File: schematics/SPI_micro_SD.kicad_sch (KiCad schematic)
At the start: 6 parts

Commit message: Файлы измененный Kicad
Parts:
- C0300: renamed from C204; footprint Capacitor_SMD:C_1206_3216Metric_Pad1.33x1.80mm_HandSolder -> Capacitor_SMD:C_0805_2012Metric
- renumbered R205 to R0300, R206 to R0301, R207 to R0302, R208 to R0303, MODULE2 to SD
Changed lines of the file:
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@@
 	(wire
 		(pts
-			(xy 140.97 102.87) (xy 146.05 102.87)
+			(xy 135.89 102.87) (xy 146.05 102.87)
 		)
 		(stroke
@@
 	(wire
 		(pts
-			(xy 140.97 100.33) (xy 146.05 100.33)
+			(xy 135.89 100.33) (xy 146.05 100.33)
 		)
 		(stroke
@@
 	(wire
 		(pts
-			(xy 140.97 107.95) (xy 146.05 107.95)
+			(xy 135.89 107.95) (xy 146.05 107.95)
 		)
 		(stroke
@@
 	(wire
 		(pts
-			(xy 140.97 113.03) (xy 146.05 113.03)
+			(xy 135.89 113.03) (xy 146.05 113.03)
 		)
 		(stroke
@@
 	(hierarchical_label "SPI_CS"
 		(shape bidirectional)
-		(at 140.97 100.33 180)
+		(at 135.89 100.33 180)
 		(effects
 			(font
@@
 	(hierarchical_label "SPI_MOSI"
 		(shape bidirectional)
-		(at 140.97 102.87 180)
+		(at 135.89 102.87 180)
 		(effects
 			(font
@@
 	(hierarchical_label "SPI_SCK"
 		(shape bidirectional)
-		(at 140.97 107.95 180)
+		(at 135.89 107.95 180)
 		(effects
 			(font
@@
 	(hierarchical_label "SPI_MISO"
 		(shape bidirectional)
-		(at 140.97 113.03 180)
+		(at 135.89 113.03 180)
 		(effects
 			(font
@@
 		(on_board yes)
 		(dnp no)
-		(property "Reference" "R206"
-			(at 143.764 101.6 90)
+		(property "Reference" "R0301"
+			(at 142.748 101.6 90)
 			(effects
 				(font
@@
 			(project "MasterBoard"
 				(path "/97e8f341-b455-4614-ab7f-cc310164e7aa/8aa098bc-8147-495f-9e0e-6764d1cf376d"
-					(reference "R206")
+					(reference "R0301")
 					(unit 1)
 				)
@@
 		(on_board yes)
 		(dnp no)
-		(property "Reference" "R207"
-			(at 143.764 106.68 90)
+		(property "Reference" "R0302"
+			(at 142.748 106.68 90)
 			(effects
 				(font
@@
 			(project "MasterBoard"
 				(path "/97e8f341-b455-4614-ab7f-cc310164e7aa/8aa098bc-8147-495f-9e0e-6764d1cf376d"
-					(reference "R207")
+					(reference "R0302")
 					(unit 1)
 				)
@@
 		(on_board yes)
 		(dnp no)
-		(property "Reference" "R205"
-			(at 143.764 99.06 90)
+		(property "Reference" "R0300"
+			(at 142.748 99.06 90)
 			(effects
 				(font
@@
 			(project "MasterBoard"
 				(path "/97e8f341-b455-4614-ab7f-cc310164e7aa/8aa098bc-8147-495f-9e0e-6764d1cf376d"
-					(reference "R205")
+					(reference "R0300")
 					(unit 1)
 				)
@@
 		(dnp no)
 		(fields_autoplaced yes)
-		(property "Reference" "C204"
+		(property "Reference" "C0300"
 			(at 118.11 109.855 0)
 			(effects
@@
 			)
 		)
-		(property "Footprint" "Capacitor_SMD:C_1206_3216Metric_Pad1.33x1.80mm_HandSolder"
+		(property "Footprint" "Capacitor_SMD:C_0805_2012Metric"
 			(at 113.3348 106.68 0)
 			(effects
@@
 			(project "MasterBoard"
 				(path "/97e8f341-b455-4614-ab7f-cc310164e7aa/8aa098bc-8147-495f-9e0e-6764d1cf376d"
-					(reference "C204")
+					(reference "C0300")
 					(unit 1)
 				)
@@
 		(on_board yes)
 		(dnp no)
-		(property "Reference" "R208"
-			(at 143.764 111.76 90)
+		(property "Reference" "R0303"
+			(at 142.748 111.76 90)
 			(effects
 				(font
@@
 			(project "MasterBoard"
 				(path "/97e8f341-b455-4614-ab7f-cc310164e7aa/8aa098bc-8147-495f-9e0e-6764d1cf376d"
-					(reference "R208")
+					(reference "R0303")
 					(unit 1)
 				)
@@
 		(on_board yes)
 		(dnp no)
-		(fields_autoplaced yes)
-		(property "Reference" "MODULE2"
-			(at 182.245 87.63 0)
+		(property "Reference" "SD"
+			(at 181.61 89.408 0)
 			(effects
 				(font
@@
 					(size 1.27 1.27)
 				)
+				(hide yes)
 			)
 		)
@@
 			(project "stm32f4_ILI_RS_SD"
 				(path "/97e8f341-b455-4614-ab7f-cc310164e7aa/8aa098bc-8147-495f-9e0e-6764d1cf376d"
-					(reference "MODULE2")
-					(unit 1)
-				)
+					(reference "SD")
+					(unit 1)
+				)

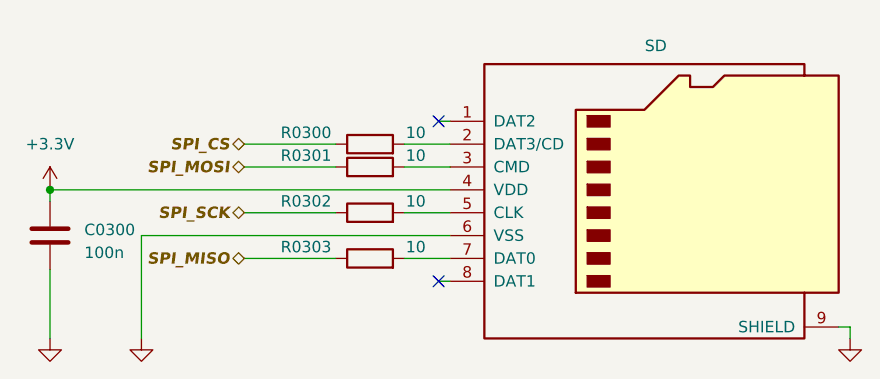
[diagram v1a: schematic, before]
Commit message: Прошелся по всей схеме: 1. почистил компоненты; 2. задал посадочные места; 3. Выставил все ссылки на плате в притык, дальнейшее расширение - смена мк
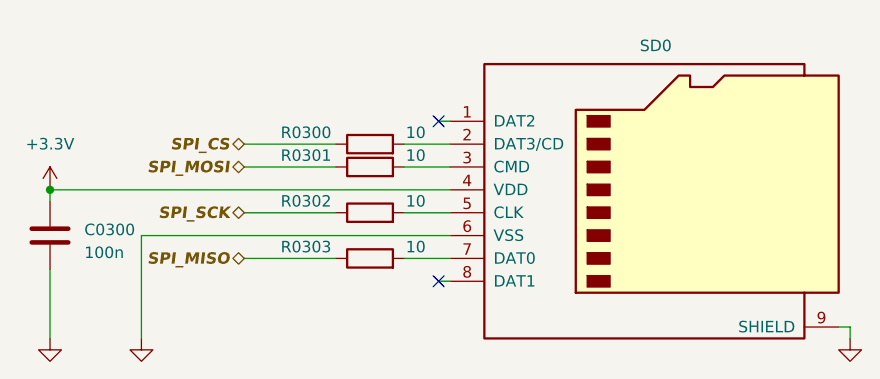
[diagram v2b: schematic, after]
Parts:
- R0300, R0301, R0302, R0303: footprint Resistor_SMD:R_1206_3216Metric_Pad1.30x1.75mm_HandSolder -> Resistor_SMD:R_0805_2012Metric
- renumbered SD to SD0
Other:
- company: (none) -> Филимонов и К
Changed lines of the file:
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@@
 	(title_block
 		(date "2025-02-25")
+		(company "Филимонов и К")
 		(comment 1 "micro-SD")
 		(comment 2 "Филимонов С.В.")
@@
 			)
 		)
-		(property "Footprint" "Resistor_SMD:R_1206_3216Metric_Pad1.30x1.75mm_HandSolder"
+		(property "Footprint" "Resistor_SMD:R_0805_2012Metric"
 			(at 149.86 104.648 90)
 			(effects
@@
 			)
 		)
-		(property "Footprint" "Resistor_SMD:R_1206_3216Metric_Pad1.30x1.75mm_HandSolder"
+		(property "Footprint" "Resistor_SMD:R_0805_2012Metric"
 			(at 149.86 109.728 90)
 			(effects
@@
 			)
 		)
-		(property "Footprint" "Resistor_SMD:R_1206_3216Metric_Pad1.30x1.75mm_HandSolder"
+		(property "Footprint" "Resistor_SMD:R_0805_2012Metric"
 			(at 149.86 102.108 90)
 			(effects
@@
 			)
 		)
-		(property "Footprint" "Resistor_SMD:R_1206_3216Metric_Pad1.30x1.75mm_HandSolder"
+		(property "Footprint" "Resistor_SMD:R_0805_2012Metric"
 			(at 149.86 114.808 90)
 			(effects
@@
 		(on_board yes)
 		(dnp no)
-		(property "Reference" "SD"
+		(property "Reference" "SD0"
 			(at 181.61 89.408 0)
 			(effects
@@
 			(project "stm32f4_ILI_RS_SD"
 				(path "/97e8f341-b455-4614-ab7f-cc310164e7aa/8aa098bc-8147-495f-9e0e-6764d1cf376d"
-					(reference "SD")
-					(unit 1)
-				)
+					(reference "SD0")
+					(unit 1)
+				)
